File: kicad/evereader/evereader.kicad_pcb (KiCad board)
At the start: 2 copper layers, 92 x 132 mm, 60 parts, among them J1 USB_C_Receptacle_USB2.0_14P, J2 Micro_SD_Card_Det1, J3 Conn_02x04_Odd_Even, J4 Conn_02x04_Odd_Even, J5 Conn_01x02, J6 Conn_01x08, J7 Conn_01x08, J8 Conn_01x02, J9 Conn_01x02, Q1 FS8205A, SW1 SW_Push, SW2 SW_Push, SW3 SW_Push, SW4 SW_Push, SW5 SW_Push, U1 TP4056-42-ESOP8, U2 DW01A, U3 AP2112K-3.3, U5 ESP32-S3-WROOM-1

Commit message: finished the PCB, finally
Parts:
- added REF**: MountingHole_2.2mm_M2, MountingHole:MountingHole_2.2mm_M2, F.Cu at (133.2, 117.6)
- added REF**: MountingHole_2.2mm_M2, MountingHole:MountingHole_2.2mm_M2, F.Cu at (133.2, 156.6)
- added REF**: MountingHole_2.2mm_M2, MountingHole:MountingHole_2.2mm_M2, F.Cu at (133.2, 31.6)
- added REF**: MouseBite-Slot_2.0x4.5mm_outset_D0.5mm_P0.85mm_7h, Panelization:MouseBite-Slot_2.0x4.5mm_outset_D0.5mm_P0.85mm_7h, F.Cu at (129.2, 152.2)
- added REF**: MountingHole_2.2mm_M2, MountingHole:MountingHole_2.2mm_M2, F.Cu at (217.3, 117.6)
- added REF**: MouseBite-Slot_2.0x4.5mm_outset_D0.5mm_P0.85mm_7h, Panelization:MouseBite-Slot_2.0x4.5mm_outset_D0.5mm_P0.85mm_7h, F.Cu at (129.2, 73.8)
- added REF**: MountingHole_2.2mm_M2, MountingHole:MountingHole_2.2mm_M2, F.Cu at (217.3, 31.4)
- added REF**: MouseBite-Slot_2.0x4.5mm_outset_D0.5mm_P0.85mm_7h, Panelization:MouseBite-Slot_2.0x4.5mm_outset_D0.5mm_P0.85mm_7h, F.Cu at (129.2, 34.5)
- added REF**: MouseBite-Slot_2.0x4.5mm_outset_D0.5mm_P0.85mm_7h, Panelization:MouseBite-Slot_2.0x4.5mm_outset_D0.5mm_P0.85mm_7h, F.Cu at (129.2, 113.0)
- added REF**: MountingHole_2.2mm_M2, MountingHole:MountingHole_2.2mm_M2, F.Cu at (217.3, 156.6)
- added REF**: MountingHole_2.2mm_M2, MountingHole:MountingHole_2.2mm_M2, F.Cu at (123.4, 156.6)
- added REF**: MountingHole_2.2mm_M2, MountingHole:MountingHole_2.2mm_M2, F.Cu at (39.2, 156.6)
- C1, C10, C12, C3, C4: value 10µF -> C15850
- C5, C6: value 1µF -> C28323
- J1: value USB_C_Receptacle_USB2.0_14P -> C165948
- J2: value Micro_SD_Card_Det1 -> C720505; footprint Connector_Card:microSD_HC_Hirose_DM3AT-SF-PEJM5 -> EasyEDA:TF-SMD_TF-115-BCP9
- J3, J4: value Conn_02x04_Odd_Even -> ~
- J5, J8: value Conn_01x02 -> C160402; footprint Connector_JST:JST_SH_SM02B-SRSS-TB_1x02-1MP_P1.00mm_Horizontal -> EasyEDA:CONN-SMD_2P-P1.00_SM02B-SRSS-TB-LF-SN
- J6, J7: value Conn_01x08 -> C160407; footprint Connector_JST:JST_SH_SM08B-SRSS-TB_1x08-1MP_P1.00mm_Horizontal -> EasyEDA:CONN-TH_SM08B-SRSS-TB-LF-SN
- J9: value Conn_01x02 -> ~
- Q1: value FS8205A -> C7525054; footprint FS8205A:SOP65P640X120-8N -> EasyEDA:TSSOP-8_L4.4-W3.0-P0.65-LS6.4-BL
- SW4, SW5: value SW_Push -> C139797
- U5: value ESP32-S3-WROOM-1 -> ESP32-S3-WROOM-1-N16-R8
- moved R13 122.3 mm to (69.6, 72.3)
- moved C15 122.3 mm to (119.6, 82.5)
- moved C14 122.2 mm to (119.6, 85.8)
- moved R12 121.9 mm to (69.6, 69.9)
- moved R14 121.6 mm to (69.6, 67.5)
- moved J7 121.0 mm to (120.4, 102.5)
- moved C6 120.4 mm to (61.9, 40.9)
- moved C7 120.4 mm to (59.7, 129.3)
- moved J3 120.4 mm to (124.2, 70.8)
- moved R10 120.4 mm to (68.3, 84.1)
- moved R11 120.4 mm to (64.1, 84.0)
- moved R17 120.4 mm to (86.6, 127.9)
- moved R19 120.4 mm to (108.3, 128.9)
- moved R4 120.4 mm to (79.7, 141.1)
- moved R5 120.4 mm to (83.7, 141.1)
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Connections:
- C16 pad 1: GND -> Net-(J4-Pin_2)
- C16 pad 2: Net-(J4-Pin_7) -> Net-(J4-Pin_1)
- C17 pad 1: GND -> Net-(J4-Pin_2)
- C17 pad 2: Net-(J4-Pin_7) -> Net-(J4-Pin_1)
- J3 pad 1: Net-(J3-Pin_1) -> GND
- J3 pad 2: Net-(J3-Pin_2) -> +3.3V
- J3 pad 7: GND -> Net-(J3-Pin_7)
- J3 pad 8: +3.3V -> Net-(J3-Pin_8)
- J6 pad 1: Net-(J4-Pin_1) -> Net-(J4-Pin_8)
- J6 pad 2: Net-(J4-Pin_2) -> Net-(J4-Pin_7)
- J6 pad 3: Net-(J4-Pin_3) -> Net-(J4-Pin_6)
- J6 pad 4: Net-(J4-Pin_4) -> Net-(J4-Pin_5)
- J6 pad 5: Net-(J4-Pin_5) -> Net-(J4-Pin_4)
- J6 pad 6: Net-(J4-Pin_6) -> Net-(J4-Pin_3)
- J6 pad 7: Net-(J4-Pin_7) -> Net-(J4-Pin_2)
- J6 pad 8: Net-(J4-Pin_8) -> Net-(J4-Pin_1)
- J7 pad 5: Net-(J3-Pin_5) -> Net-(J3-Pin_3)
- J7 pad 6: Net-(J3-Pin_6) -> Net-(J3-Pin_4)
- J9 pad 1: Net-(J8-Pin_1) -> Net-(J8-Pin_2)
- J9 pad 2: Net-(J8-Pin_2) -> Net-(J8-Pin_1)
- SW5 pad 2: +3.3V -> Net-(U5-EN)
- U1 pad 9: unconnected-(U1-EPAD-Pad9) -> GND
- U5 pad 17: Net-(J3-Pin_3) -> Net-(J3-Pin_5)
- U5 pad 18: Net-(J3-Pin_4) -> Net-(J3-Pin_6)
- U5 pad 19: Net-(J3-Pin_6) -> Net-(J3-Pin_4)
- U5 pad 20: Net-(J3-Pin_5) -> Net-(J3-Pin_3)
- U5 pad 4: Net-(J3-Pin_1) -> Net-(J3-Pin_7)
- U5 pad 5: Net-(J3-Pin_2) -> Net-(J3-Pin_8)
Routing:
- net Net-(U5-IO1): track 16.9 -> 155.9 mm, vias 1 -> 2
- net Net-(U5-IO2): track 16.3 -> 124.6 mm, vias 1 -> 3
- net +3.3V: track 314.0 -> 415.7 mm, vias 9 -> 12
- net Net-(J3-Pin_7): track 0.00 -> 74.6 mm, vias 0 -> 1
- net Net-(J3-Pin_8): track 0.00 -> 73.7 mm, vias 0 -> 3
- net Net-(J3-Pin_1): track 64.4 -> 0.00 mm, vias 1 -> 0
- net Net-(J3-Pin_2): track 61.3 -> 0.00 mm, vias 1 -> 0
- net Net-(J4-Pin_1): track 0.00 -> 38.2 mm
- net Net-(J4-Pin_8): track 0.00 -> 36.8 mm, vias 0 -> 1
- net Net-(J4-Pin_6): track 0.00 -> 34.1 mm, vias 0 -> 1
- net Net-(J4-Pin_7): track 0.00 -> 33.9 mm, vias 0 -> 1
- net Net-(J4-Pin_5): track 0.00 -> 33.1 mm
- net Net-(J4-Pin_3): track 0.00 -> 31.8 mm, vias 0 -> 1
- net Net-(J4-Pin_2): track 0.00 -> 30.3 mm
- net Net-(J4-Pin_4): track 0.00 -> 29.9 mm, vias 0 -> 1
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- added copper zone on B.Cu, net GND
- added copper zone on F.Cu, net GND
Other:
- board size 92 x 132 mm -> 186 x 132 mm
- board text added: "B- B+"
- board text added: "EVEREADER"
- board text added: "USB_C_R"

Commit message: fixed up some stuff on the PCB
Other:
- board text added: "100uF"

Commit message: fixed jst connector having inverted wiring on the pcb and added nomenclatures for each component
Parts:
- moved C14 0.11 mm to (119.6, 85.9)
- moved C15 0.11 mm to (119.6, 82.6)
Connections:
- C16 pad 1: Net-(J4-Pin_2) -> GND
- C16 pad 2: Net-(J4-Pin_1) -> +3.3V
- C17 pad 1: Net-(J4-Pin_2) -> GND
- C17 pad 2: Net-(J4-Pin_1) -> +3.3V
- J4 pad 1: Net-(J4-Pin_1) -> +3.3V
- J4 pad 2: Net-(J4-Pin_2) -> GND
- J4 pad 3: Net-(J4-Pin_3) -> Net-(J3-Pin_4)
- J4 pad 4: Net-(J4-Pin_4) -> Net-(J3-Pin_3)
- J6 pad 1: Net-(J4-Pin_8) -> +3.3V
- J6 pad 2: Net-(J4-Pin_7) -> GND
- J6 pad 3: Net-(J4-Pin_6) -> Net-(J3-Pin_4)
- J6 pad 4: Net-(J4-Pin_5) -> Net-(J3-Pin_3)
- J6 pad 5: Net-(J4-Pin_4) -> Net-(J4-Pin_5)
- J6 pad 6: Net-(J4-Pin_3) -> Net-(J4-Pin_6)
- J6 pad 7: Net-(J4-Pin_2) -> Net-(J4-Pin_7)
- J6 pad 8: Net-(J4-Pin_1) -> Net-(J4-Pin_8)
- J7 pad 1: Net-(J7-Pin_1) -> Net-(J4-Pin_8)
- J7 pad 2: Net-(J7-Pin_2) -> Net-(J4-Pin_7)
- J7 pad 3: Net-(J7-Pin_3) -> Net-(J4-Pin_6)
- J7 pad 4: Net-(J7-Pin_4) -> Net-(J4-Pin_5)
- J8 pad 1: Net-(J8-Pin_1) -> Net-(J5-Pin_2)
- J8 pad 2: Net-(J8-Pin_2) -> Net-(J5-Pin_1)
- J9 pad 1: Net-(J8-Pin_2) -> Net-(J5-Pin_1)
- J9 pad 2: Net-(J8-Pin_1) -> Net-(J5-Pin_2)
- U5 pad 11: Net-(J7-Pin_1) -> Net-(J4-Pin_8)
- U5 pad 12: Net-(J7-Pin_3) -> Net-(J4-Pin_6)
- U5 pad 7: Net-(J7-Pin_4) -> Net-(J4-Pin_5)
- U5 pad 8: Net-(J7-Pin_2) -> Net-(J4-Pin_7)
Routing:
- net Net-(J4-Pin_7): track 33.9 -> 132.0 mm, vias 1 -> 2
- net Net-(J4-Pin_8): track 36.8 -> 132.6 mm, vias 1 -> 3
- net Net-(J7-Pin_2): track 93.8 -> 0.00 mm, vias 2 -> 0
- net Net-(J7-Pin_1): track 87.4 -> 0.00 mm, vias 2 -> 0
- net Net-(J4-Pin_6): track 34.1 -> 114.9 mm, vias 1 -> 2
- net Net-(J4-Pin_5): track 33.1 -> 113.6 mm, vias 0 -> 2
- net Net-(J7-Pin_3): track 79.8 -> 0.00 mm, vias 2 -> 0
- net Net-(J7-Pin_4): track 79.6 -> 0.00 mm, vias 2 -> 0
- net Net-(J4-Pin_1): track 38.2 -> 0.00 mm
- net Net-(J4-Pin_3): track 31.8 -> 0.00 mm, vias 1 -> 0
- net Net-(J4-Pin_2): track 30.3 -> 0.00 mm
- net Net-(J3-Pin_3): track 84.3 -> 114.6 mm, vias 2 -> 3
- net Net-(J4-Pin_4): track 29.9 -> 0.00 mm, vias 1 -> 0
- net Net-(J3-Pin_4): track 82.0 -> 111.6 mm, vias 4 -> 5
- net GND: track 482.1 -> 507.4 mm
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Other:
- board text added: "01x02_1mm_JST_SH"
- board text added: "02x04_1mm_JST_SH"
- board text added: "1.2kΩ"
- board text added: "100nF"
- board text added: "100Ω"
- board text added: "10kΩ"
- board text added: "10nF"
- board text added: "10μF"
- board text added: "1MΩ"
- board text added: "1kΩ"
- board text added: "1μF"
- board text added: "2-PIN_SWITCH"
- board text added: "4_PIN_SWITCH"
- board text added: "5.1kΩ"
- board text added: "AP2112K 3.3"
- board text added: "DW01A"
- board text added: "ESP32-S3-WROOM-1-N16R8"
- board text added: "FS8205A"
- board text added: "GREEN_LED"
- board text added: "MICRO_SD_CARD_READER"
- board text added: "RED_LED"
- board text added: "TP4056"
- board text added: "USB_C_REC"
- board text removed: "USB_C_R"

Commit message: added keepout zone i had previously removed from esp32
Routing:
- net GND: track 507.4 -> 513.2 mm
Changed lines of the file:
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@@
 		(sheetname "/")
 		(sheetfile "evereader.kicad_sch")
-		(units
-			(unit
-				(name "A")
-				(pins "3" "27" "39" "38" "15" "4" "5" "6" "7" "12" "17" "18" "19" "20"
-					"21" "22" "8" "9" "2" "41" "40" "1" "37" "36" "10" "11" "13" "14" "23"
-					"28" "29" "30" "31" "32" "33" "34" "35" "26" "16" "24" "25"
-				)
-			)
-		)
 		(attr smd)
 		(duplicate_pad_numbers_are_jumpers no)
@@
 		)
 		(fp_line
+			(start -13 -6.75)
+			(end -13 -18)
+			(stroke
+				(width 0.05)
+				(type default)
+			)
+			(layer "F.CrtYd")
+		)
+		(fp_line
 			(start -9.75 -6.75)
-			(end -9.75 -13.5)
+			(end -13 -6.75)
 			(stroke
 				(width 0.05)
@@
 		)
 		(fp_line
-			(start 9.75 -13.5)
-			(end -9.75 -13.5)
+			(start 9.75 -6.75)
+			(end 9.75 13.45)
+			(stroke
+				(width 0.05)
+				(type solid)
+			)
+			(layer "F.CrtYd")
+		)
+		(fp_line
+			(start 9.75 -6.75)
+			(end 13 -6.75)
 			(stroke
 				(width 0.05)
@@
 		)
 		(fp_line
-			(start 9.75 -6.75)
-			(end 9.75 -13.5)
+			(start 13 -18)
+			(end -13 -18)
 			(stroke
 				(width 0.05)
@@
 		)
 		(fp_line
-			(start 9.75 -6.75)
-			(end 9.75 13.45)
+			(start 13 -6.75)
+			(end 13 -18)
 			(stroke
 				(width 0.05)
-				(type solid)
+				(type default)
 			)
 			(layer "F.CrtYd")
@@
 			(zone_connect 2)
 		)
+		(zone
+			(layers "F.Cu" "B.Cu")
+			(name "ESP_KEEP_OUT")
+			(hatch edge 0.5)
+			(connect_pads
+				(clearance 0)
+			)
+			(min_thickness 0.25)
+			(keepout
+				(tracks not_allowed)
+				(vias not_allowed)
+				(pads not_allowed)
+				(copperpour not_allowed)
+				(footprints not_allowed)
+			)
+			(placement
+				(enabled no)
+				(sheetname "/")
+			)
+			(fill
+				(thermal_gap 0.5)
+				(thermal_bridge_width 0.5)
+				(island_removal_mode 0)
+			)
+			(polygon
+				(pts
+					(xy 93.578287 34.547918) (xy 93.578287 24.547918) (xy 68.578287 24.547918) (xy 68.578287 34.547918)
+				)
+			)
+		)
 		(embedded_fonts no)
 		(model "${KICAD10_3DMODEL_DIR}/RF_Module.3dshapes/ESP32-S3-WROOM-1.step"
@@
 	)
 	(segment
+		(start 136.9 80.46)
+		(end 136.9 80.44)
+		(width 0.5)
+		(layer "B.Cu")
+		(net "GND")
+	)
+	(segment
 		(start 77.181471 137.27)
 		(end 85.141471 137.27)
@@
 	)
 	(segment
+		(start 136.8 76.42)
+		(end 136.8 76.4)
+		(width 0.5)
+		(layer "B.Cu")
+		(net "GND")
+	)
+	(segment
 		(start 66.09 80.97)
 		(end 72.185 74.875)
@@
 	)
 	(segment
+		(start 134.84 78.38)
+		(end 136.9 80.44)
+		(width 0.5)
+		(layer "B.Cu")
+		(net "GND")
+	)
+	(segment
 		(start 55.921471 144.16)
 		(end 55.921471 145.31)
@@
 		(width 0.5)
 		(layer "B.Cu")
+		(net "GND")
+	)
+	(segment
+		(start 134.84 78.38)
+		(end 136.8 76.42)
+		(width 0.5)
+		(layer "B.Cu")

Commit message: fixed up PCB schematics component values
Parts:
- added C18: 100nF, Capacitor_SMD:C_0805_2012Metric, F.Cu at (95.0, 56.6)
- added C19: 100nF, Capacitor_SMD:C_0805_2012Metric, F.Cu at (63.0, 55.7)
- C1, C10, C12, C3, C4: value C15850 -> 10μF
- C5, C6: value C28323 -> 1μF
- J1: value C165948 -> USB-C-2.0-RECEPTACLE
- J2: value C720505 -> MICRO-SD-CARD-READER
- J5, J8: value C160402 -> JST_SH_01x02_1.0mm
- J6, J7: value C160407 -> JST_SH_02x04_1.0mm
- Q1: value C7525054 -> FS8205A
- SW4, SW5: value C139797 -> 2_PIN_SW
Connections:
- C16 pad 1: GND -> Net-(J4-Pin_2)
- C16 pad 2: +3.3V -> Net-(J4-Pin_1)
- C17 pad 1: GND -> Net-(J4-Pin_2)
- C17 pad 2: +3.3V -> Net-(J4-Pin_1)
- J4 pad 1: +3.3V -> Net-(J4-Pin_1)
- J4 pad 2: GND -> Net-(J4-Pin_2)
- J4 pad 3: Net-(J3-Pin_4) -> Net-(J4-Pin_3)
- J4 pad 4: Net-(J3-Pin_3) -> Net-(J4-Pin_4)
- J6 pad 1: +3.3V -> Net-(J4-Pin_1)
- J6 pad 2: GND -> Net-(J4-Pin_2)
- J6 pad 3: Net-(J3-Pin_4) -> Net-(J4-Pin_3)
- J6 pad 4: Net-(J3-Pin_3) -> Net-(J4-Pin_4)
- J7 pad 1: Net-(J4-Pin_8) -> Net-(J7-Pin_1)
- J7 pad 2: Net-(J4-Pin_7) -> Net-(J7-Pin_2)
- J7 pad 3: Net-(J4-Pin_6) -> Net-(J7-Pin_3)
- J7 pad 4: Net-(J4-Pin_5) -> Net-(J7-Pin_4)
- J8 pad 1: Net-(J5-Pin_2) -> Net-(J8-Pin_1)
- J8 pad 2: Net-(J5-Pin_1) -> Net-(J8-Pin_2)
- J9 pad 1: Net-(J5-Pin_1) -> Net-(J8-Pin_2)
- J9 pad 2: Net-(J5-Pin_2) -> Net-(J8-Pin_1)
- U5 pad 11: Net-(J4-Pin_8) -> Net-(J7-Pin_1)
- U5 pad 12: Net-(J4-Pin_6) -> Net-(J7-Pin_3)
- U5 pad 7: Net-(J4-Pin_5) -> Net-(J7-Pin_4)
- U5 pad 8: Net-(J4-Pin_7) -> Net-(J7-Pin_2)
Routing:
- net Net-(J7-Pin_2): track 0.00 -> 93.8 mm, vias 0 -> 2
- net Net-(J4-Pin_7): track 132.0 -> 38.2 mm, vias 2 -> 0
- net Net-(J7-Pin_1): track 0.00 -> 87.4 mm, vias 0 -> 2
- net Net-(J4-Pin_8): track 132.6 -> 45.2 mm, vias 3 -> 1
- net Net-(J7-Pin_3): track 0.00 -> 79.8 mm, vias 0 -> 2
- net Net-(J4-Pin_6): track 114.9 -> 35.1 mm, vias 2 -> 0
- net Net-(J7-Pin_4): track 0.00 -> 79.6 mm, vias 0 -> 2
- net Net-(J4-Pin_5): track 113.6 -> 34.0 mm, vias 2 -> 0
- net Net-(J4-Pin_2): track 0.00 -> 31.0 mm
- net Net-(J3-Pin_3): track 114.6 -> 84.3 mm, vias 3 -> 2
- net Net-(J4-Pin_4): track 0.00 -> 30.3 mm, vias 0 -> 1
- net Net-(J3-Pin_4): track 111.6 -> 82.0 mm, vias 5 -> 4
- net Net-(J4-Pin_3): track 0.00 -> 29.6 mm, vias 0 -> 1
- net Net-(J4-Pin_1): track 0.00 -> 22.9 mm
- net +3.3V: track 438.8 -> 415.9 mm
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
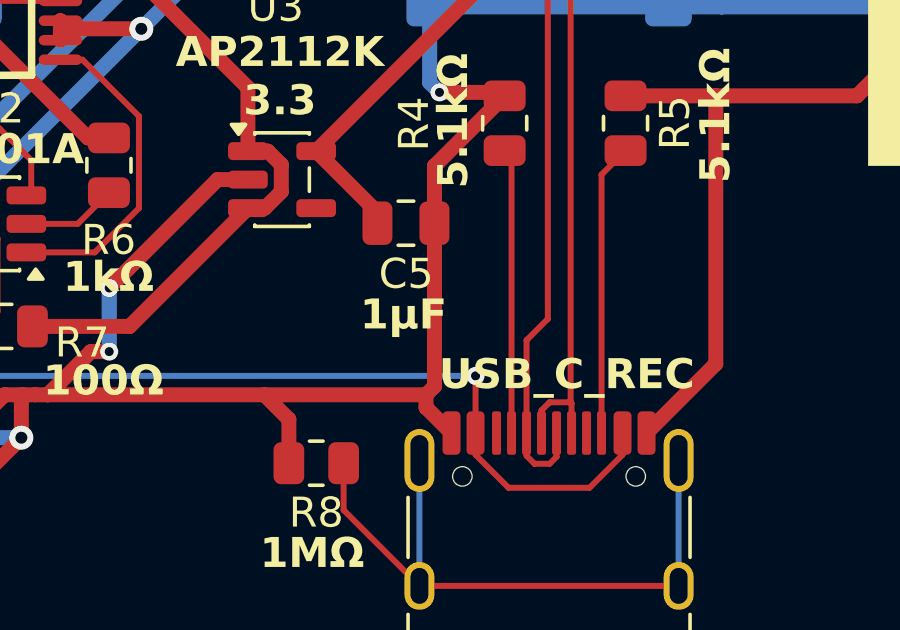
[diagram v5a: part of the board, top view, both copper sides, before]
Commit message: made ldo 1uF capacitor a 100uF
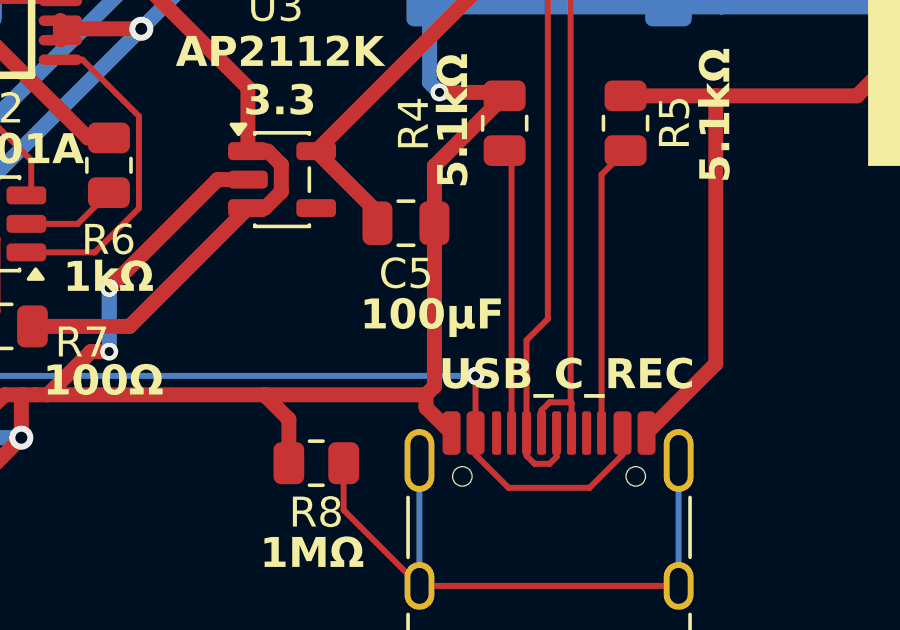
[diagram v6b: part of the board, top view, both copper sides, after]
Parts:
- C5: value 1μF -> 100μF
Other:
- board text added: "100μF"
